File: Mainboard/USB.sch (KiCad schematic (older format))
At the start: 23 parts, among them J8 USB_B_Micro, U3 LP5907MFX-3.3, U8 FE1.1s-BQFN24B, Y2 12MHz

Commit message: Modify library references
As described in the README of the newly added libraries submodule.
Schematic and PCB are synced.

Hardware folder is renamed to mainboard
Any other PCBs can be put in their own subfolder in the gitrepo

Commit also swaps source/drain of Q1 because it appeared wrong for some
reason after updating all symbol/footprints.
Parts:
- U8: symbol ZOUDIOsymbols:FE1.1s-BQFN24B -> ZOUDIO-symbols:FE1.1s-BQFN24B
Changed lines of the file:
@@
 3.3V LDO
 $Comp
-L ZOUDIOsymbols:FE1.1s-BQFN24B U8
+L ZOUDIO-symbols:FE1.1s-BQFN24B U8
 U 1 1 610AB39B
 P 5400 4150

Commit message: Add USB-C
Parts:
- added P1: USB_C_Plug_USB2.0, Connector_USB:USB_C_Receptacle_Palconn_UTC16-G, symbol Connector:USB_C_Plug_USB2.0
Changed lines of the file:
@@
+	1    0    0    -1
+$EndComp
+$Comp
+L Connector:USB_C_Plug_USB2.0 P1
+U 1 1 6161D587
+P 1550 3850
+F 0 "P1" H 1700 4750 50  0000 C CNN
+F 1 "USB_C_Plug_USB2.0" H 1700 4650 50  0000 C CNN
+F 2 "Connector_USB:USB_C_Receptacle_Palconn_UTC16-G" H 1700 3850 50  0001 C CNN
+F 3 "https://www.usb.org/sites/default/files/documents/usb_type-c.zip" H 1700 3850 50  0001 C CNN
+	1    1550 3850
 	1    0    0    -1
 $EndComp

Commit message: Before power tree change
Backup before switching from two to one LDO
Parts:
- removed J8: USB_B_Micro, Connector_USB:USB_Micro-B_Molex-105017-0001, symbol Connector:USB_B_Micro
- removed P1: USB_C_Plug_USB2.0, Connector_USB:USB_C_Receptacle_Palconn_UTC16-G, symbol Connector:USB_C_Plug_USB2.0
- added J?: USB-C, symbol Connector:USB_C_Receptacle_USB2.0
- added R? (x2): 5.1k, Resistor_SMD:R_0603_1608Metric, symbol Device:R_Small
- R21: value 1k -> 10k
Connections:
- net labels added: D+, D-, VBUS
- net labels removed: 5V_usb
- wire segments 83 -> 100
- no-connect marks 7 -> 8
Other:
- note added: "Hub controller"
- note added: "USB-C receptacle"
- note removed: "USB hub controller"
- moved on the sheet: F1, FB1

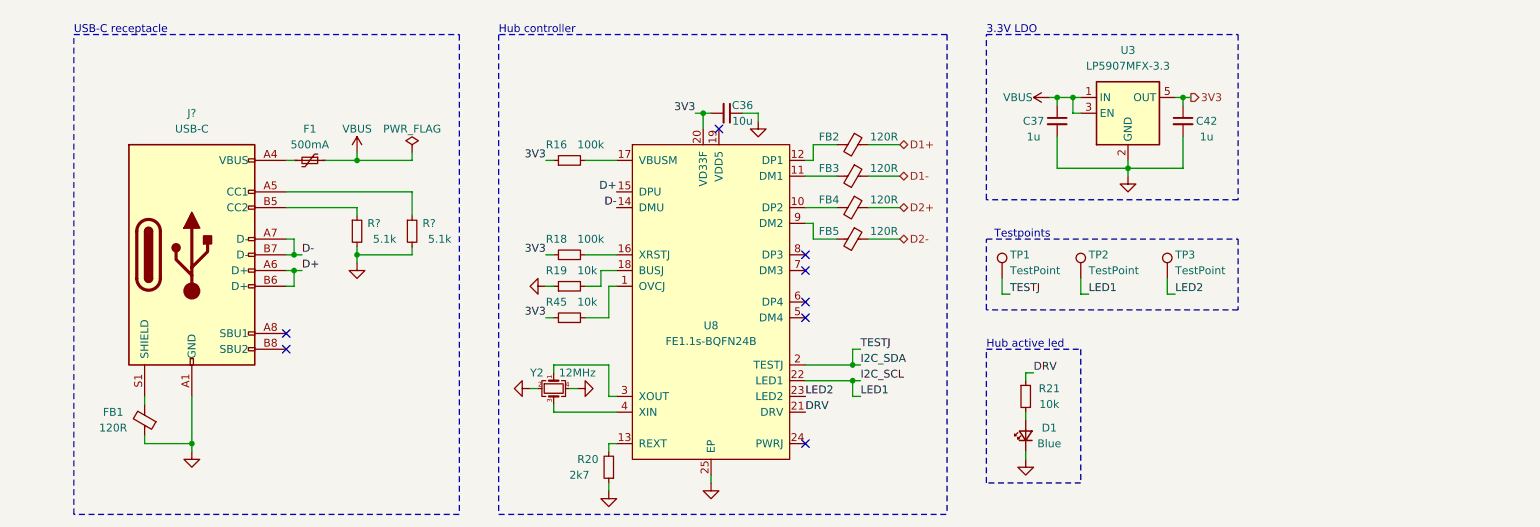
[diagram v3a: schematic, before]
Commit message: Before testing CH340B and VCHG
Cleaned up amp lay-out a bit in the meanwhile
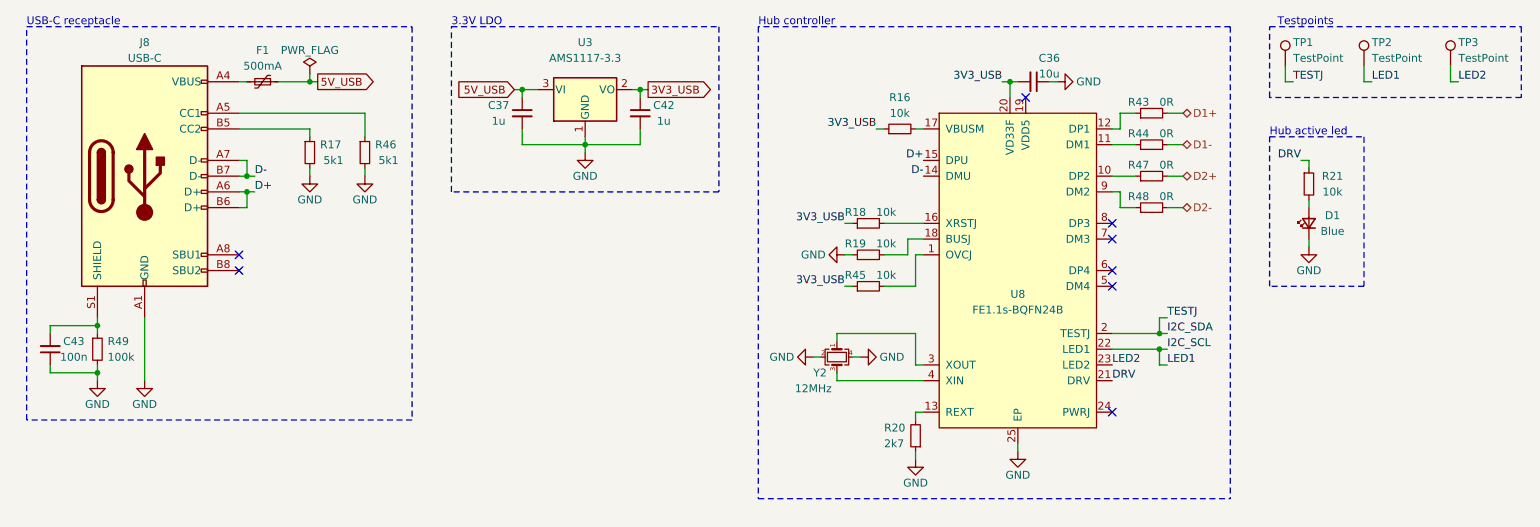
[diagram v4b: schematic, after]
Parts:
- removed FB1, FB2, FB3, FB4, FB5: 120R, Capacitor_SMD:C_0603_1608Metric, symbol Device:Ferrite_Bead_Small
- removed R?: 5.1k, Resistor_SMD:R_0603_1608Metric, symbol Device:R_Small
- removed U3: LP5907MFX-3.3, Package_TO_SOT_SMD:SOT-23-5, symbol Regulator_Linear:LP5907MFX-3.3
- added C43: 100n, Capacitor_SMD:C_0603_1608Metric, symbol Device:C_Small
- added R43, R44, R47, R48: 0R, Resistor_SMD:R_0603_1608Metric, symbol Device:R_Small
- added R46: 5k1, Resistor_SMD:R_0603_1608Metric, symbol Device:R_Small
- added R49: 100k, Resistor_SMD:R_0603_1608Metric, symbol Device:R_Small
- added U3: AMS1117-3.3, Package_TO_SOT_SMD:SOT-223-3_TabPin2, symbol Regulator_Linear:AMS1117-3.3
- C37, C42: Manufacturer (none) -> Taiyo Yuden; Partnumber (none) -> UMK212B7105KG-T
- J8: renamed from J?; footprint (none) -> Connector_USB:USB_C_Receptacle_Palconn_UTC16-G
- R16, R18: value 100k -> 10k
- R17: renamed from R?; value 5.1k -> 5k1
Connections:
- net D1+: now also R43.2
- net D1-: now also R44.2
- net D2+: now also R47.2
- net D2-: now also R48.2
- net GND: now also C43.1, R46.2, R49.2, U3.1 (GND)
- net at U8.11 (DM1): now also R44.1
- net at U8.12 (DP1): now also R43.1
- net at U8.9 (DM2): now also R48.1
- net at U8.10 (DP2): now also R47.1
- net at J8.S1 (SHIELD): now also C43.2, R49.1
- net at J8.A5 (CC1): now also R46.1
- net 3V3 renamed 3V3_USB
- net 3V3_USB: now also U3.2 (VO)
- net VBUS renamed 5V_USB
- net 5V_USB: now also U3.3 (VI)
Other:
- moved on the sheet: C36, C37, C42, D1, F1, J8, R17, R20, R21, R45, TP1, TP2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

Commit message: Result after weekend of lay-out
Pretty far, just neats to be cleaned up for production.
Does not pass DRC yet.
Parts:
- U8: footprint Package_DFN_QFN:QFN-24-1EP_4x4mm_P0.5mm_EP2.6x2.6mm_ThermalVias -> Package_DFN_QFN:QFN-24-1EP_4x4mm_P0.5mm_EP2.6x2.6mm
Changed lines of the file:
@@
 F 0 "U8" H 7350 3800 50  0000 C CNN
 F 1 "FE1.1s-BQFN24B" H 7350 3700 50  0000 C CNN
-F 2 "Package_DFN_QFN:QFN-24-1EP_4x4mm_P0.5mm_EP2.6x2.6mm_ThermalVias" H 7350 4000 50  0001 C CNN
+F 2 "Package_DFN_QFN:QFN-24-1EP_4x4mm_P0.5mm_EP2.6x2.6mm" H 7350 4000 50  0001 C CNN
 F 3 "" H 7350 4000 50  0001 C CNN
 	1    7350 3950

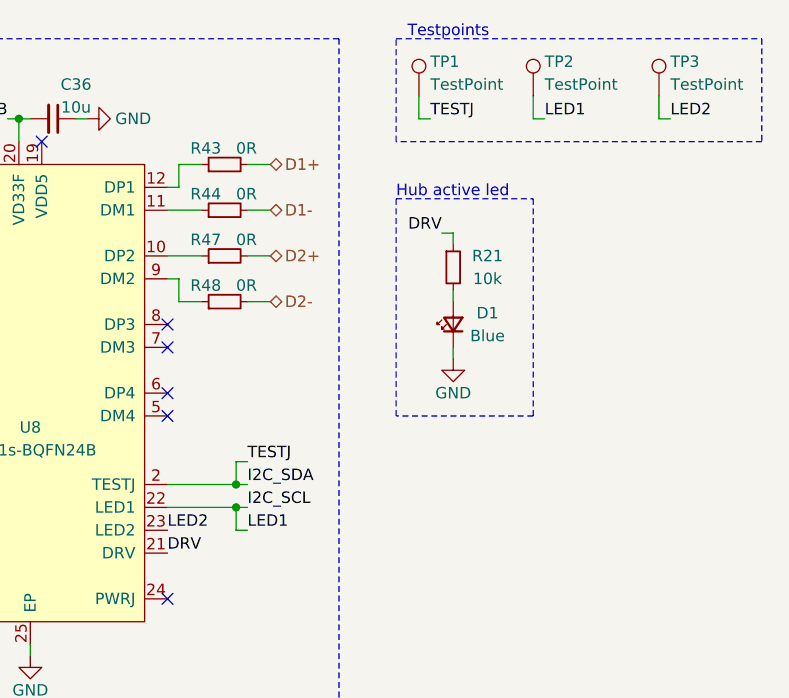
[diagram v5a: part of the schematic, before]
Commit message: Mainboard: Version 1.0
Still need to clean up 3D models and BoM list,
but gerberexport-ready and ready to order.
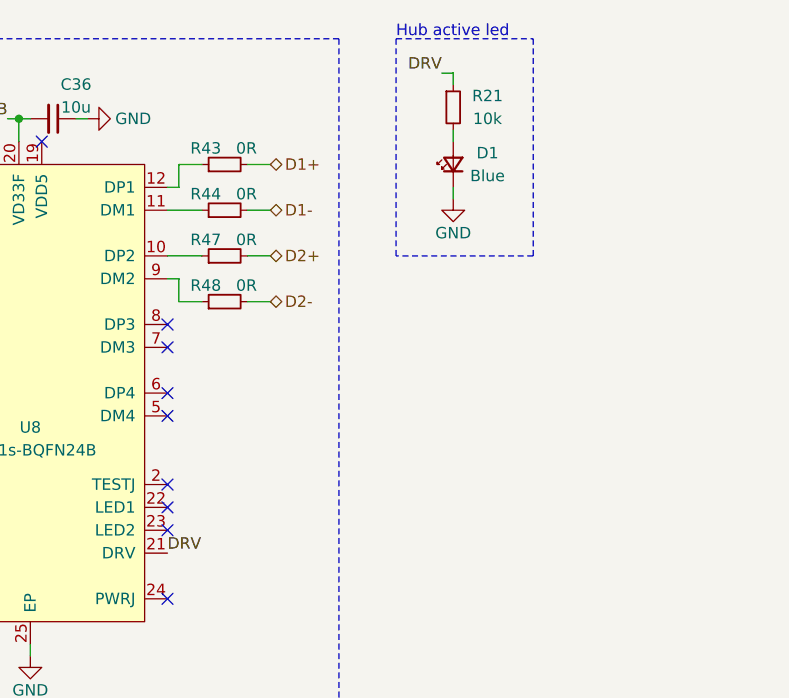
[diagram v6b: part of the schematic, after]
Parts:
- removed TP1, TP2, TP3: TestPoint, TestPoint:TestPoint_Pad_D1.0mm, symbol Connector:TestPoint
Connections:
- net I2C_SCL: no longer names the net of U8.22 (LED1)
- net I2C_SDA: no longer names the net of U8.2 (TESTJ)
- net LED2: no longer names the net of U8.23 (LED2)
- no-connect marks 8 -> 11
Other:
- note removed: "Testpoints"
- moved on the sheet: D1, R21
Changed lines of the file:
@@
 Sheet 7 11
 Title "4x38W amp with DSP and BT"
-Date "2021-11-19"
-Rev "0.2"
+Date "2021-12-01"
+Rev "1.0"
 Comp "ZOUDIO"
 Comment1 ""
@@
 Wire Wire Line
 	6700 5100 6700 5150
-Text Label 8300 4350 0    50   ~ 0
-I2C_SDA
-Text Label 8300 4450 0    50   ~ 0
-I2C_SCL
 NoConn ~ 7950 4850
-Text Label 7950 4550 0    50   ~ 0
-LED2
-Text Label 7950 4650 0    50   ~ 0
-DRV
-Wire Wire Line
-	8300 4450 8250 4450
-Text Label 10150 2750 0    50   ~ 0
-LED2
 Wire Wire Line
 	6300 3850 6250 3850
@@
 	6700 4550 6750 4550
 Wire Wire Line
-	8250 4450 7950 4450
-Connection ~ 8250 4450
-Text Label 8300 4550 0    50   ~ 0
-LED1
-Wire Wire Line
 	8100 3150 7950 3150
 Wire Wire Line
@@
 Wire Wire Line
 	6250 3650 6300 3650
-Wire Wire Line
-	8250 4450 8250 4550
-Wire Wire Line
-	8300 4550 8250 4550
-Wire Wire Line
-	8300 4350 8250 4350
-Wire Notes Line
-	8950 3100 9550 3100
-Wire Notes Line
-	9550 3100 9550 4050
-Wire Notes Line
-	9550 4050 8950 4050
-Wire Notes Line
-	8950 4050 8950 3100
-Text Notes 8950 3100 0    50   ~ 0
+Wire Notes Line
+	8950 2400 9550 2400
+Wire Notes Line
+	9550 2400 9550 3350
+Wire Notes Line
+	9550 3350 8950 3350
+Wire Notes Line
+	8950 3350 8950 2400
+Text Notes 8950 2400 0    50   ~ 0
 Hub active led
 Wire Wire Line
@@
 Wire Wire Line
 	6700 4350 6700 4550
-Text Label 8300 4250 0    50   ~ 0
-TESTJ
-Wire Wire Line
-	8300 4250 8250 4250
-Wire Wire Line
-	8250 4250 8250 4350
-Connection ~ 8250 4350
-Wire Wire Line
-	8250 4350 7950 4350
 $Comp
 L Device:C_Small C36
@@
 Wire Wire Line
 	7300 2750 7300 2850
-Text Label 9150 3250 2    50   ~ 0
+Text Label 9150 2550 2    50   ~ 0
 DRV
 Wire Wire Line
-	9200 3250 9200 3300
+	9200 2550 9200 2600
 $Comp
 L Device:R_Small R21
 U 1 1 60C9D1DB
-P 9200 3400
-F 0 "R21" H 9350 3450 50  0000 C CNN
-F 1 "10k" H 9350 3350 50  0000 C CNN
-F 2 "Resistor_SMD:R_0603_1608Metric" H 9200 3400 50  0001 C CNN
-F 3 "~" H 9200 3400 50  0001 C CNN
-	1    9200 3400
-	1    0    0    -1
-$EndComp
-Wire Wire Line
-	9200 3500 9200 3550
-Wire Wire Line
-	9200 3750 9200 3800
+P 9200 2700
+F 0 "R21" H 9350 2750 50  0000 C CNN
+F 1 "10k" H 9350 2650 50  0000 C CNN
+F 2 "Resistor_SMD:R_0603_1608Metric" H 9200 2700 50  0001 C CNN
+F 3 "~" H 9200 2700 50  0001 C CNN
+	1    9200 2700
+	1    0    0    -1
+$EndComp
+Wire Wire Line
+	9200 2800 9200 2850
+Wire Wire Line
+	9200 3050 9200 3100
 $Comp
 L Device:LED_Small D?
 U 1 1 60C62FEE
-P 9200 3650
+P 9200 2950
 AR Path="/60BB5CE1/60C62FEE" Ref="D?"  Part="1"
 AR Path="/60E45FC0/60C62FEE" Ref="D1"  Part="1"
-F 0 "D1" V 9250 3500 50  0000 C CNN
-F 1 "Blue" V 9150 3500 50  0000 C CNN
-F 2 "LED_SMD:LED_0603_1608Metric" V 9200 3650 50  0001 C CNN
-F 3 "~" V 9200 3650 50  0001 C CNN
-F 4 "Orient" H 9200 3650 50  0001 C CNN "Manufacturer"
-F 5 "ORH-B36G" H 9200 3650 50  0001 C CNN "Partnumber"
-	1    9200 3650
-	0    -1   -1   0
-$EndComp
-$Comp
-L Connector:TestPoint TP3
-U 1 1 60CCAB94
-P 10100 2650
-F 0 "TP3" H 10150 2800 50  0000 L CNN
-F 1 "TestPoint" H 10150 2700 50  0000 L CNN
-F 2 "TestPoint:TestPoint_Pad_D1.0mm" H 10300 2650 50  0001 C CNN
-F 3 "~" H 10300 2650 50  0001 C CNN
-	1    10100 2650
-	1    0    0    -1
-$EndComp
-Wire Wire Line
-	10100 2650 10100 2750
-Wire Wire Line
-	10100 2750 10150 2750
-Wire Notes Line
-	8950 2400 10550 2400
-Wire Notes Line
-	10550 2400 10550 2850
-Wire Notes Line
-	10550 2850 8950 2850
-Wire Notes Line
-	8950 2850 8950 2400
-Text Notes 9000 2400 0    50   ~ 0
-Testpoints
-$Comp
-L Connector:TestPoint TP1
-U 1 1 60D11389
-P 9050 2650
-F 0 "TP1" H 9100 2800 50  0000 L CNN
-F 1 "TestPoint" H 9100 2700 50  0000 L CNN
-F 2 "TestPoint:TestPoint_Pad_D1.0mm" H 9250 2650 50  0001 C CNN
-F 3 "~" H 9250 2650 50  0001 C CNN
-	1    9050 2650
-	1    0    0    -1
-$EndComp
-Wire Wire Line
-	9100 2750 9050 2750
-Wire Wire Line
-	9050 2750 9050 2650
-$Comp
-L Connector:TestPoint TP2
-U 1 1 60D11396
-P 9550 2650
-F 0 "TP2" H 9600 2800 50  0000 L CNN
-F 1 "TestPoint" H 9600 2700 50  0000 L CNN
-F 2 "TestPoint:TestPoint_Pad_D1.0mm" H 9750 2650 50  0001 C CNN
-F 3 "~" H 9750 2650 50  0001 C CNN
-	1    9550 2650
-	1    0    0    -1
-$EndComp
-Wire Wire Line
-	9550 2650 9550 2750
-Wire Wire Line
-	9550 2750 9600 2750
-Text Label 9100 2750 0    50   ~ 0
-TESTJ
-Text Label 9600 2750 0    50   ~ 0
-LED1
+F 0 "D1" V 9250 2800 50  0000 C CNN
+F 1 "Blue" V 9150 2800 50  0000 C CNN
+F 2 "LED_SMD:LED_0603_1608Metric" V 9200 2950 50  0001 C CNN
+F 3 "~" V 9200 2950 50  0001 C CNN
+F 4 "Orient" H 9200 2950 50  0001 C CNN "Manufacturer"
+F 5 "ORH-B36G" H 9200 2950 50  0001 C CNN "Partnumber"
+	1    9200 2950
+	0    -1   -1   0
+$EndComp
 $Comp
 L Device:Polyfuse_Small F1
@@
 L power:GND #PWR011
 U 1 1 619E6C77
-P 9200 3800
-F 0 "#PWR011" H 9200 3550 50  0001 C CNN
-F 1 "GND" H 9200 3650 50  0000 C CNN
-F 2 "" H 9200 3800 50  0001 C CNN
-F 3 "" H 9200 3800 50  0001 C CNN
-	1    9200 3800
+P 9200 3100
+F 0 "#PWR011" H 9200 2850 50  0001 C CNN
+F 1 "GND" H 9200 2950 50  0000 C CNN
+F 2 "" H 9200 3100 50  0001 C CNN
+F 3 "" H 9200 3100 50  0001 C CNN
+	1    9200 3100
 	1    0    0    -1
 $EndComp
@@
 $EndComp
 Wire Wire Line
-	9150 3250 9200 3250
+	9150 2550 9200 2550
 $Comp
 L power:GND #PWR0142
@@
 	1500 4600 1500 4650
 Connection ~ 1500 4600
+NoConn ~ 7950 4550
+NoConn ~ 7950 4450
+NoConn ~ 7950 4350
+Text Label 7950 4650 0    50   ~ 0
+DRV
 $EndSCHEMATC

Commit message: Clean up schematic for BoM export
- Change 22u 0805's (amp decoupling) to 15u
- Change 680n 0805's (part of output filter) to 470n
- Change C1 (amp bulk cap) from 820u to 1000u
- Add BoM.ini for KiBom export and
- Complete fields needed for KiBom (Manufacturer and partnumber)
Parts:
- C36: Manufacturer (none) -> Samsung; Partnumber (none) -> CL21A106KPFNNNG
- D1: Manufacturer Orient -> Wurth; Partnumber ORH-B36G -> 150060BS75000
- F1: Manufacturer (none) -> Eaton; Partnumber (none) -> PTS12066V050
- J8: Manufacturer (none) -> GCT; Partnumber (none) -> USB4105-GF-A
- R16, R18, R19, R21, R45: Manufacturer (none) -> Yageo; Partnumber (none) -> RC0603FR-0710KL
- R17, R46: Manufacturer (none) -> Yageo; Partnumber (none) -> RC0603FR-075K1L
- R20: Manufacturer (none) -> Yageo; Partnumber (none) -> RC0603FR-072K7L
- R43, R44, R47, R48: Manufacturer (none) -> Yageo; Partnumber (none) -> RC0603FR-070RL
- R49: Manufacturer (none) -> Yageo; Partnumber (none) -> RC0603FR-07100KL
- U3: Manufacturer (none) -> Diodes Inc; Partnumber (none) -> AZ1117IH-3.3TRG1
- U8: value FE1.1s-BQFN24B -> FE1.1S; Manufacturer (none) -> Terminus; Partnumber (none) -> FE1.1s-BQFN24B
- Y2: Manufacturer (none) -> ECS; Partnumber (none) -> ECS-120-20-30B-AEN-TR
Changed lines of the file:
@@
 F 2 "Resistor_SMD:R_0603_1608Metric" H 6700 5000 50  0001 C CNN
 F 3 "~" H 6700 5000 50  0001 C CNN
+F 4 "Yageo" H 6700 5000 50  0001 C CNN "Manufacturer"
+F 5 "RC0603FR-072K7L" H 6700 5000 50  0001 C CNN "Partnumber"
 	1    6700 5000
 	-1   0    0    1
@@
 F 2 "Capacitor_SMD:C_0805_2012Metric" H 7450 2750 50  0001 C CNN
 F 3 "~" H 7450 2750 50  0001 C CNN
+F 4 "Samsung" H 7450 2750 50  0001 C CNN "Manufacturer"
+F 5 "CL21A106KPFNNNG" H 7450 2750 50  0001 C CNN "Partnumber"
 	1    7450 2750
 	0    1    1    0
@@
 F 2 "Resistor_SMD:R_0603_1608Metric" H 9200 2700 50  0001 C CNN
 F 3 "~" H 9200 2700 50  0001 C CNN
+F 4 "Yageo" H 9200 2700 50  0001 C CNN "Manufacturer"
+F 5 "RC0603FR-0710KL" H 9200 2700 50  0001 C CNN "Partnumber"
 	1    9200 2700
 	1    0    0    -1
@@
 F 2 "LED_SMD:LED_0603_1608Metric" V 9200 2950 50  0001 C CNN
 F 3 "~" V 9200 2950 50  0001 C CNN
-F 4 "Orient" H 9200 2950 50  0001 C CNN "Manufacturer"
-F 5 "ORH-B36G" H 9200 2950 50  0001 C CNN "Partnumber"
+F 4 "Wurth" H 9200 2950 50  0001 C CNN "Manufacturer"
+F 5 "150060BS75000" H 9200 2950 50  0001 C CNN "Partnumber"
 	1    9200 2950
 	0    -1   -1   0
@@
 F 2 "Fuse:Fuse_1206_3216Metric" H 2600 2550 50  0001 L CNN
 F 3 "~" H 2550 2750 50  0001 C CNN
+F 4 "Eaton" H 2550 2750 50  0001 C CNN "Manufacturer"
+F 5 "PTS12066V050" H 2550 2750 50  0001 C CNN "Partnumber"
 	1    2550 2750
 	0    1    1    0
@@
 F 2 "Resistor_SMD:R_0603_1608Metric" H 6400 4050 50  0001 C CNN
 F 3 "~" H 6400 4050 50  0001 C CNN
+F 4 "Yageo" H 6400 4050 50  0001 C CNN "Manufacturer"
+F 5 "RC0603FR-0710KL" H 6400 4050 50  0001 C CNN "Partnumber"
 	1    6400 4050
 	0    -1   -1   0
@@
 F 2 "Connector_USB:USB_C_Receptacle_Palconn_UTC16-G" H 1950 3350 50  0001 C CNN
 F 3 "https://www.usb.org/sites/default/files/documents/usb_type-c.zip" H 1950 3350 50  0001 C CNN
+F 4 "GCT" H 1800 3350 50  0001 C CNN "Manufacturer"
+F 5 "USB4105-GF-A" H 1800 3350 50  0001 C CNN "Partnumber"
 	1    1800 3350
 	1    0    0    -1
@@
 F 2 "Resistor_SMD:R_0603_1608Metric" H 2850 3200 50  0001 C CNN
 F 3 "~" H 2850 3200 50  0001 C CNN
+F 4 "Yageo" H 2850 3200 50  0001 C CNN "Manufacturer"
+F 5 "RC0603FR-075K1L" H 2850 3200 50  0001 C CNN "Partnumber"
 	1    2850 3200
 	1    0    0    -1
@@
 F 2 "Resistor_SMD:R_0603_1608Metric" H 3200 3200 50  0001 C CNN
 F 3 "~" H 3200 3200 50  0001 C CNN
+F 4 "Yageo" H 3200 3200 50  0001 C CNN "Manufacturer"
+F 5 "RC0603FR-075K1L" H 3200 3200 50  0001 C CNN "Partnumber"
 	1    3200 3200
 	1    0    0    -1
@@
 F 2 "Resistor_SMD:R_0603_1608Metric" H 6400 3850 50  0001 C CNN
 F 3 "~" H 6400 3850 50  0001 C CNN
+F 4 "Yageo" H 6400 3850 50  0001 C CNN "Manufacturer"
+F 5 "RC0603FR-0710KL" H 6400 3850 50  0001 C CNN "Partnumber"
 	1    6400 3850
 	0    -1   -1   0
@@
 F 2 "Resistor_SMD:R_0603_1608Metric" H 6400 3650 50  0001 C CNN
 F 3 "~" H 6400 3650 50  0001 C CNN
+F 4 "Yageo" H 6400 3650 50  0001 C CNN "Manufacturer"
+F 5 "RC0603FR-0710KL" H 6400 3650 50  0001 C CNN "Partnumber"
 	1    6400 3650
 	0    -1   -1   0
@@
 F 2 "Resistor_SMD:R_0603_1608Metric" H 6600 3050 50  0001 C CNN
 F 3 "~" H 6600 3050 50  0001 C CNN
+F 4 "Yageo" H 6600 3050 50  0001 C CNN "Manufacturer"
+F 5 "RC0603FR-0710KL" H 6600 3050 50  0001 C CNN "Partnumber"
 	1    6600 3050
 	0    -1   -1   0
@@
 P 7350 3950
 F 0 "U8" H 7350 3800 50  0000 C CNN
-F 1 "FE1.1s-BQFN24B" H 7350 3700 50  0000 C CNN
+F 1 "FE1.1S" H 7350 3700 50  0000 C CNN
 F 2 "Package_DFN_QFN:QFN-24-1EP_4x4mm_P0.5mm_EP2.6x2.6mm" H 7350 4000 50  0001 C CNN
 F 3 "" H 7350 4000 50  0001 C CNN
+F 4 "Terminus" H 7350 3950 50  0001 C CNN "Manufacturer"
+F 5 "FE1.1s-BQFN24B" H 7350 3950 50  0001 C CNN "Partnumber"
 	1    7350 3950
 	1    0    0    -1
@@
 F 2 "Crystal:Crystal_SMD_Abracon_ABM3C-4Pin_5.0x3.2mm" H 6200 4500 50  0001 C CNN
 F 3 "~" H 6200 4500 50  0001 C CNN
+F 4 "ECS" H 6200 4500 50  0001 C CNN "Manufacturer"
+F 5 "ECS-120-20-30B-AEN-TR" H 6200 4500 50  0001 C CNN "Partnumber"
 	1    6200 4500
 	0    1    1    0
@@
 F 2 "Package_TO_SOT_SMD:SOT-223-3_TabPin2" H 4600 3000 50  0001 C CNN
 F 3 "http://www.advanced-monolithic.com/pdf/ds1117.pdf" H 4700 2550 50  0001 C CNN
+F 4 "Diodes Inc" H 4600 2800 50  0001 C CNN "Manufacturer"
+F 5 "AZ1117IH-3.3TRG1" H 4600 2800 50  0001 C CNN "Partnumber"
 	1    4600 2800
 	1    0    0    -1
@@
 F 2 "Resistor_SMD:R_0603_1608Metric" H 8200 2950 50  0001 C CNN
 F 3 "~" H 8200 2950 50  0001 C CNN
+F 4 "Yageo" H 8200 2950 50  0001 C CNN "Manufacturer"
+F 5 "RC0603FR-070RL" H 8200 2950 50  0001 C CNN "Partnumber"
 	1    8200 2950
 	0    -1   -1   0
@@
 F 2 "Resistor_SMD:R_0603_1608Metric" H 8200 3150 50  0001 C CNN
 F 3 "~" H 8200 3150 50  0001 C CNN
+F 4 "Yageo" H 8200 3150 50  0001 C CNN "Manufacturer"
+F 5 "RC0603FR-070RL" H 8200 3150 50  0001 C CNN "Partnumber"
 	1    8200 3150
 	0    -1   -1   0
@@
 F 2 "Resistor_SMD:R_0603_1608Metric" H 8200 3350 50  0001 C CNN
 F 3 "~" H 8200 3350 50  0001 C CNN
+F 4 "Yageo" H 8200 3350 50  0001 C CNN "Manufacturer"
+F 5 "RC0603FR-070RL" H 8200 3350 50  0001 C CNN "Partnumber"
 	1    8200 3350
 	0    -1   -1   0
@@
 F 2 "Resistor_SMD:R_0603_1608Metric" H 8200 3550 50  0001 C CNN
 F 3 "~" H 8200 3550 50  0001 C CNN
+F 4 "Yageo" H 8200 3550 50  0001 C CNN "Manufacturer"
+F 5 "RC0603FR-070RL" H 8200 3550 50  0001 C CNN "Partnumber"
 	1    8200 3550
 	0    -1   -1   0
@@
 F 2 "Resistor_SMD:R_0603_1608Metric" H 1500 4450 50  0001 C CNN
 F 3 "~" H 1500 4450 50  0001 C CNN
+F 4 "Yageo" H 1500 4450 50  0001 C CNN "Manufacturer"
+F 5 "RC0603FR-07100KL" H 1500 4450 50  0001 C CNN "Partnumber"
 	1    1500 4450
 	1    0    0    -1
